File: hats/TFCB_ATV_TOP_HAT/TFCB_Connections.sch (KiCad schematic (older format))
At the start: 5 parts

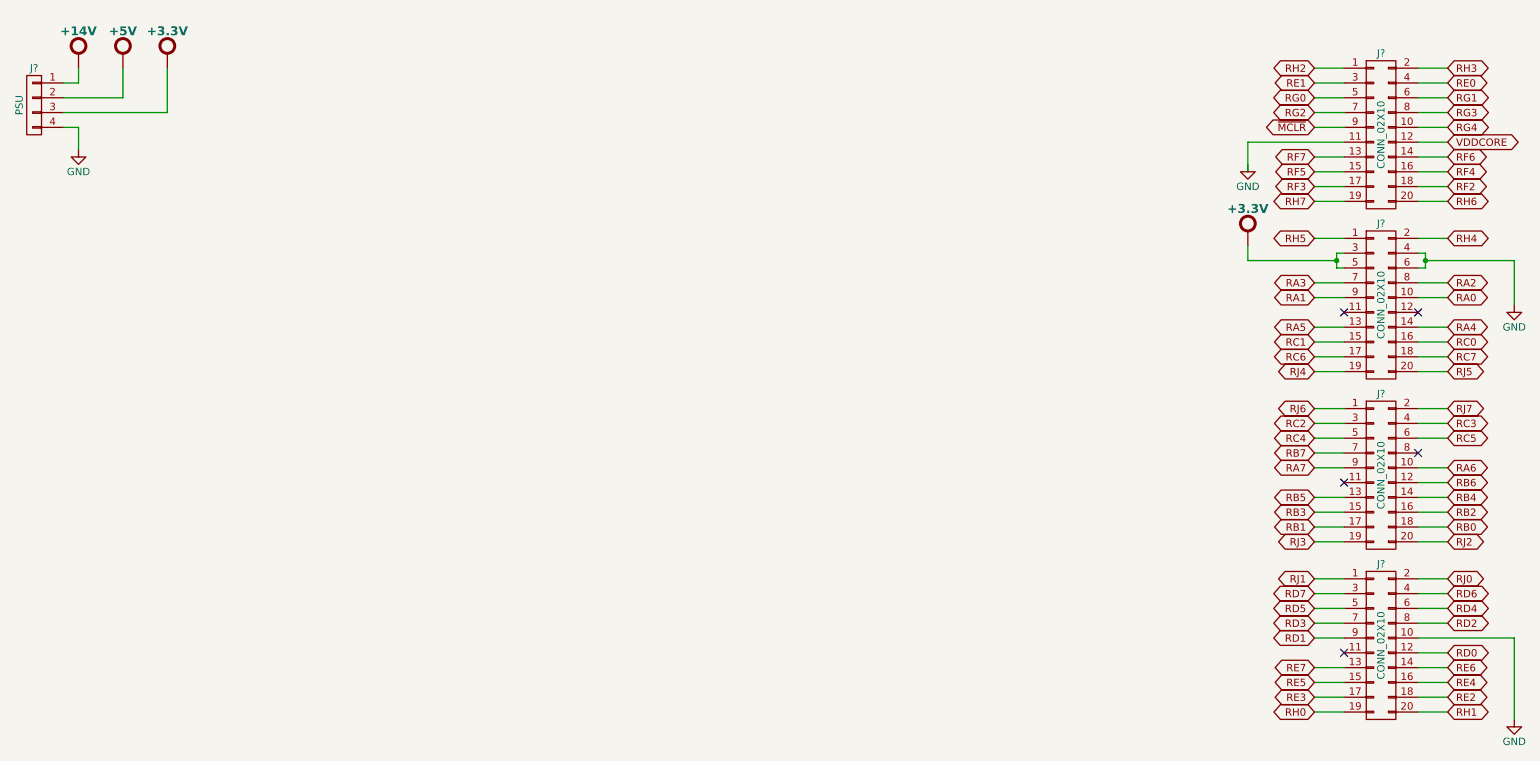
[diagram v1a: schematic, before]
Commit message: Added scanner trigger and current sense cct
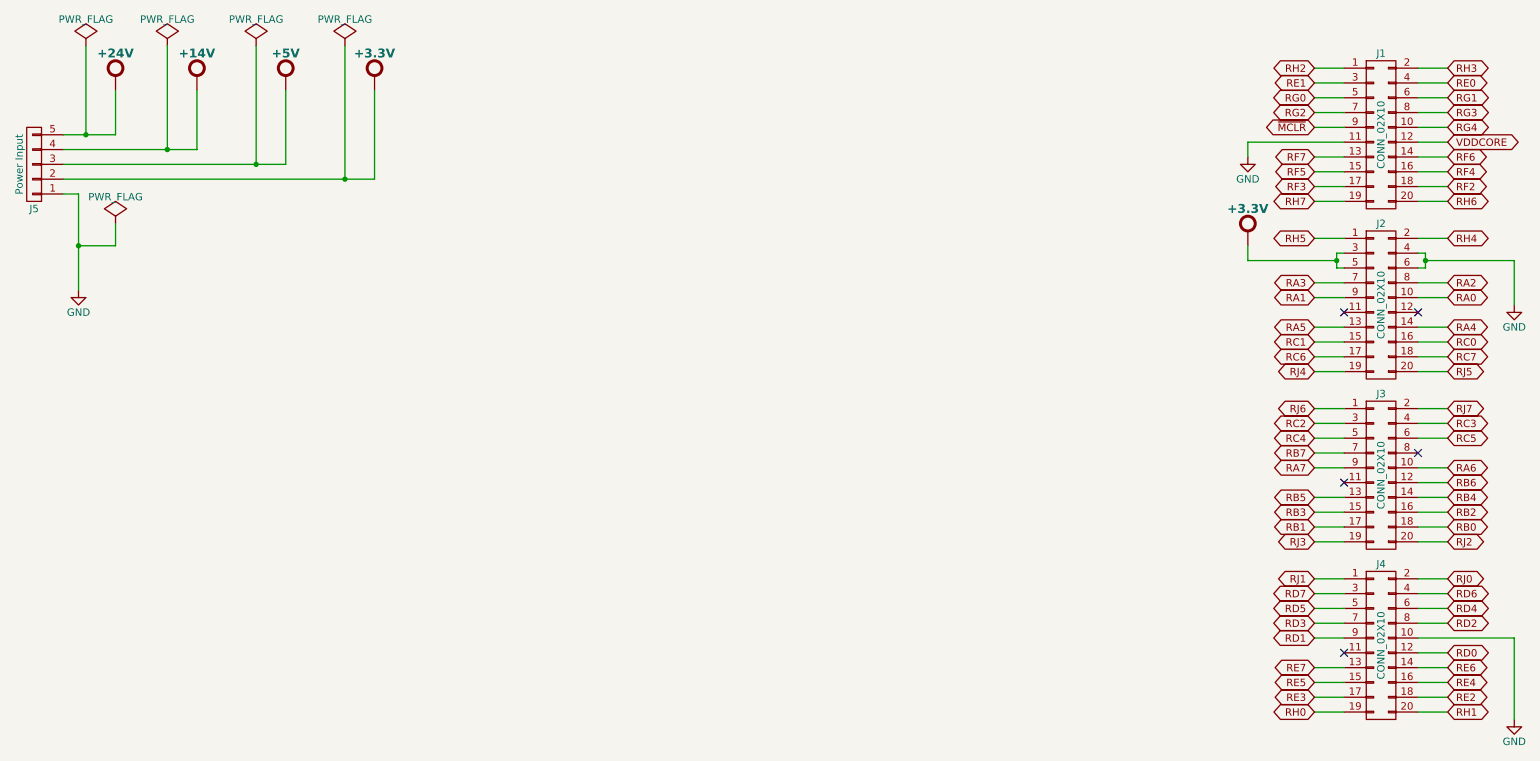
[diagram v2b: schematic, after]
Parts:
- removed J?: PSU, symbol CONN_01X04
- added J5: Power Input, bjh-kicad-connector-fp:Weidmuller-SL-5.08-Vertical-5Pole, symbol CONN_01X05
- J1, J2, J3, J4: renamed from J?; footprint (none) -> bjh-kicad-connector-fp:RCPT-2row-2.54mm-10way
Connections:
- net +14V: now also J5.4 (P4)
- net +3.3V: now also J5.2 (P2)
- net +5V: now also J5.3 (P3)
- net GND: now also J1.11 (P11), J5.1 (P1)
- new net +24V: J5.5 (P5)
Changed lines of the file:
@@
 LIBS:contrib
 LIBS:valves
+LIBS:buzzer
+LIBS:Relays
+LIBS:PowerSymbols-BJH
+LIBS:Oscillators-BJH
+LIBS:Microchip-BJH
+LIBS:LCD-BJH
+LIBS:Devices-BJH
+LIBS:Connectors-BJH
 LIBS:Basics-BJH
-LIBS:buzzer
-LIBS:Connectors-BJH
-LIBS:Devices-BJH
-LIBS:LCD-BJH
-LIBS:Microchip-BJH
-LIBS:Oscillators-BJH
-LIBS:PowerSymbols-BJH
-LIBS:Relays
+LIBS:Transistors-BJH
 LIBS:TFCB_ATV_HAT-cache
 EELAYER 25 0
@@
 $Descr A4 11693 8268
 encoding utf-8
-Sheet 2 7
+Sheet 2 6
 Title "TFCB CONNECTIONS"
 Date "Wed 24 Jun 2015"
@@
 $EndDescr
 $Comp
-L CONN_02X10 J?
+L CONN_02X10 J1
 U 1 1 558930FC
 P 9800 1350
-F 0 "J?" H 9800 1900 50  0000 C CNN
+F 0 "J1" H 9800 1900 50  0000 C CNN
 F 1 "CONN_02X10" V 9800 1350 50  0000 C CNN
-F 2 "" H 9800 150 60  0000 C CNN
+F 2 "bjh-kicad-connector-fp:RCPT-2row-2.54mm-10way" H 9800 150 60  0001 C CNN
 F 3 "" H 9800 150 60  0000 C CNN
 	1    9800 1350
@@
 $EndComp
 $Comp
-L CONN_02X10 J?
+L CONN_02X10 J2
 U 1 1 558931C8
 P 9800 2500
-F 0 "J?" H 9800 3050 50  0000 C CNN
+F 0 "J2" H 9800 3050 50  0000 C CNN
 F 1 "CONN_02X10" V 9800 2500 50  0000 C CNN
-F 2 "" H 9800 1300 60  0000 C CNN
+F 2 "bjh-kicad-connector-fp:RCPT-2row-2.54mm-10way" H 9800 1300 60  0001 C CNN
 F 3 "" H 9800 1300 60  0000 C CNN
 	1    9800 2500
@@
 $EndComp
 $Comp
-L CONN_02X10 J?
+L CONN_02X10 J3
 U 1 1 5589321A
 P 9800 3650
-F 0 "J?" H 9800 4200 50  0000 C CNN
+F 0 "J3" H 9800 4200 50  0000 C CNN
 F 1 "CONN_02X10" V 9800 3650 50  0000 C CNN
-F 2 "" H 9800 2450 60  0000 C CNN
+F 2 "bjh-kicad-connector-fp:RCPT-2row-2.54mm-10way" H 9800 2450 60  0001 C CNN
 F 3 "" H 9800 2450 60  0000 C CNN
 	1    9800 3650
@@
 $EndComp
 $Comp
-L CONN_02X10 J?
+L CONN_02X10 J4
 U 1 1 55893262
 P 9800 4800
-F 0 "J?" H 9800 5350 50  0000 C CNN
+F 0 "J4" H 9800 5350 50  0000 C CNN
 F 1 "CONN_02X10" V 9800 4800 50  0000 C CNN
-F 2 "" H 9800 3600 60  0000 C CNN
+F 2 "bjh-kicad-connector-fp:RCPT-2row-2.54mm-10way" H 9800 3600 60  0001 C CNN
 F 3 "" H 9800 3600 60  0000 C CNN
 	1    9800 4800
@@
 RH1
 $Comp
-L GND #PWR?
+L GND #PWR01
 U 1 1 55894D4F
 P 10700 5300
-F 0 "#PWR?" H 10700 5050 50  0001 C CNN
+F 0 "#PWR01" H 10700 5050 50  0001 C CNN
 F 1 "GND" H 10700 5150 50  0000 C CNN
 F 2 "" H 10700 5300 60  0000 C CNN
@@
 $EndComp
 $Comp
-L GND #PWR?
+L GND #PWR02
 U 1 1 55894EE0
 P 10700 2500
-F 0 "#PWR?" H 10700 2250 50  0001 C CNN
+F 0 "#PWR02" H 10700 2250 50  0001 C CNN
 F 1 "GND" H 10700 2350 50  0000 C CNN
 F 2 "" H 10700 2500 60  0000 C CNN
@@
 $EndComp
 $Comp
-L +3.3V_BJH #PWR?
+L +3.3V_BJH #PWR03
 U 1 1 558AB965
 P 8900 2050
-F 0 "#PWR?" H 8900 2240 20  0001 C CNN
+F 0 "#PWR03" H 8900 2240 20  0001 C CNN
 F 1 "+3.3V_BJH" H 8900 2240 51  0001 C CNN
 F 2 "" H 8900 2050 60  0001 C CNN
@@
 	1    0    0    -1
 $EndComp
+$Comp
+L GND #PWR04
+U 1 1 558ABA4F
+P 8900 1500
+F 0 "#PWR04" H 8900 1250 50  0001 C CNN
+F 1 "GND" H 8900 1350 50  0000 C CNN
+F 2 "" H 8900 1500 60  0000 C CNN
+F 3 "" H 8900 1500 60  0000 C CNN
+	1    8900 1500
+	1    0    0    -1
+$EndComp
+$Comp
+L +14V_BJH #PWR05
+U 1 1 558ABE2B
+P 1800 1000
+F 0 "#PWR05" H 1800 1190 20  0001 C CNN
+F 1 "+14V_BJH" H 1800 1190 51  0001 C CNN
+F 2 "" H 1800 1000 60  0001 C CNN
+F 3 "" H 1800 1000 60  0001 C CNN
+F 4 "+14V" H 1800 1200 60  0000 C CNB "NAME"
+	1    1800 1000
+	1    0    0    -1
+$EndComp
+$Comp
+L +5V_BJH #PWR06
+U 1 1 558ABE4F
+P 2400 1000
+F 0 "#PWR06" H 2400 1190 20  0001 C CNN
+F 1 "+5V_BJH" H 2400 1190 51  0001 C CNN
+F 2 "" H 2400 1000 60  0001 C CNN
+F 3 "" H 2400 1000 60  0001 C CNN
+F 4 "+5V" H 2400 1200 60  0000 C CNB "NAME"
+	1    2400 1000
+	1    0    0    -1
+$EndComp
+$Comp
+L +3.3V_BJH #PWR07
+U 1 1 558ABE73
+P 3000 1000
+F 0 "#PWR07" H 3000 1190 20  0001 C CNN
+F 1 "+3.3V_BJH" H 3000 1190 51  0001 C CNN
+F 2 "" H 3000 1000 60  0001 C CNN
+F 3 "" H 3000 1000 60  0001 C CNN
+F 4 "+3.3V" H 3000 1200 60  0000 C CNB "NAME"
+	1    3000 1000
+	1    0    0    -1
+$EndComp
+$Comp
+L GND #PWR08
+U 1 1 558ABF2A
+P 1000 2400
+F 0 "#PWR08" H 1000 2150 50  0001 C CNN
+F 1 "GND" H 1000 2250 50  0000 C CNN
+F 2 "" H 1000 2400 60  0000 C CNN
+F 3 "" H 1000 2400 60  0000 C CNN
+	1    1000 2400
+	1    0    0    -1
+$EndComp
 Wire Wire Line
 	9350 900  9550 900
@@
 	8900 2200 9500 2200
 Connection ~ 9500 2200
-$Comp
-L GND #PWR?
-U 1 1 558ABA4F
-P 8900 1550
-F 0 "#PWR?" H 8900 1300 50  0001 C CNN
-F 1 "GND" H 8900 1400 50  0000 C CNN
-F 2 "" H 8900 1550 60  0000 C CNN
-F 3 "" H 8900 1550 60  0000 C CNN
-	1    8900 1550
-	1    0    0    -1
-$EndComp
-Wire Wire Line
-	8900 1600 8900 1400
 Wire Wire Line
 	8900 1400 9550 1400
-$Comp
-L CONN_01X04 J?
-U 1 1 558ABD6E
-P 700 1150
-F 0 "J?" H 700 1400 50  0000 C CNN
-F 1 "PSU" V 800 1150 50  0000 C CNN
-F 2 "" H 700 1150 60  0000 C CNN
-F 3 "" H 700 1150 60  0000 C CNN
-	1    700  1150
-	-1   0    0    -1
-$EndComp
-$Comp
-L +14V_BJH #PWR?
-U 1 1 558ABE2B
-P 1000 850
-F 0 "#PWR?" H 1000 1040 20  0001 C CNN
-F 1 "+14V_BJH" H 1000 1040 51  0001 C CNN
-F 2 "" H 1000 850 60  0001 C CNN
-F 3 "" H 1000 850 60  0001 C CNN
-F 4 "+14V" H 1000 1050 60  0000 C CNB "NAME"
-	1    1000 850
-	1    0    0    -1
-$EndComp
-$Comp
-L +5V_BJH #PWR?
-U 1 1 558ABE4F
-P 1300 850
-F 0 "#PWR?" H 1300 1040 20  0001 C CNN
-F 1 "+5V_BJH" H 1300 1040 51  0001 C CNN
-F 2 "" H 1300 850 60  0001 C CNN
-F 3 "" H 1300 850 60  0001 C CNN
-F 4 "+5V" H 1300 1050 60  0000 C CNB "NAME"
-	1    1300 850
-	1    0    0    -1
-$EndComp
-$Comp
-L +3.3V_BJH #PWR?
-U 1 1 558ABE73
-P 1600 850
-F 0 "#PWR?" H 1600 1040 20  0001 C CNN
-F 1 "+3.3V_BJH" H 1600 1040 51  0001 C CNN
-F 2 "" H 1600 850 60  0001 C CNN
-F 3 "" H 1600 850 60  0001 C CNN
-F 4 "+3.3V" H 1600 1050 60  0000 C CNB "NAME"
-	1    1600 850
-	1    0    0    -1
-$EndComp
-$Comp
-L GND #PWR?
-U 1 1 558ABF2A
-P 1000 1450
-F 0 "#PWR?" H 1000 1200 50  0001 C CNN
-F 1 "GND" H 1000 1300 50  0000 C CNN
-F 2 "" H 1000 1450 60  0000 C CNN
-F 3 "" H 1000 1450 60  0000 C CNN
-	1    1000 1450
-	1    0    0    -1
-$EndComp
-Wire Wire Line
-	900  1300 1000 1300
-Wire Wire Line
-	1000 1300 1000 1450
-Wire Wire Line
-	1000 900  1000 1000
-Wire Wire Line
-	1000 1000 900  1000
-Wire Wire Line
-	1300 900  1300 1100
-Wire Wire Line
-	1300 1100 900  1100
-Wire Wire Line
-	1600 900  1600 1200
-Wire Wire Line
-	1600 1200 900  1200
+Wire Wire Line
+	900  1750 1000 1750
+Wire Wire Line
+	1000 1750 1000 2400
+Wire Wire Line
+	900  1450 1800 1450
+Wire Wire Line
+	900  1550 2400 1550
+Wire Wire Line
+	900  1650 3000 1650
+Wire Wire Line
+	1800 1450 1800 1050
+Wire Wire Line
+	2400 1550 2400 1050
+Wire Wire Line
+	3000 1650 3000 1050
+$Comp
+L PWR_FLAG #FLG09
+U 1 1 55B023D2
+P 1600 750
+F 0 "#FLG09" H 1600 845 50  0001 C CNN
+F 1 "PWR_FLAG" H 1600 930 50  0000 C CNN
+F 2 "" H 1600 750 60  0000 C CNN
+F 3 "" H 1600 750 60  0000 C CNN
+	1    1600 750
+	1    0    0    -1
+$EndComp
+Wire Wire Line
+	1600 750  1600 1450
+Connection ~ 1600 1450
+$Comp
+L PWR_FLAG #FLG010
+U 1 1 55B02455
+P 2200 750
+F 0 "#FLG010" H 2200 845 50  0001 C CNN
+F 1 "PWR_FLAG" H 2200 930 50  0000 C CNN
+F 2 "" H 2200 750 60  0000 C CNN
+F 3 "" H 2200 750 60  0000 C CNN
+	1    2200 750
+	1    0    0    -1
+$EndComp
+$Comp
+L PWR_FLAG #FLG011
+U 1 1 55B02473
+P 2800 750
+F 0 "#FLG011" H 2800 845 50  0001 C CNN
+F 1 "PWR_FLAG" H 2800 930 50  0000 C CNN
+F 2 "" H 2800 750 60  0000 C CNN
+F 3 "" H 2800 750 60  0000 C CNN
+	1    2800 750
+	1    0    0    -1
+$EndComp
+Wire Wire Line
+	2200 750  2200 1550
+Connection ~ 2200 1550
+Wire Wire Line
+	2800 750  2800 1650
+Connection ~ 2800 1650
+$Comp
+L PWR_FLAG #FLG012
+U 1 1 55B026DF
+P 1250 1950
+F 0 "#FLG012" H 1250 2045 50  0001 C CNN
+F 1 "PWR_FLAG" H 1250 2130 50  0000 C CNN
+F 2 "" H 1250 1950 60  0000 C CNN
+F 3 "" H 1250 1950 60  0000 C CNN
+	1    1250 1950
+	1    0    0    -1
+$EndComp
+Wire Wire Line
+	1250 1950 1250 2100
+Wire Wire Line
+	1250 2100 1000 2100
+Connection ~ 1000 2100
+Wire Wire Line
+	8900 1400 8900 1500
+$Comp
+L CONN_01X05 J5
+U 1 1 55B22208
+P 700 1550
+F 0 "J5" H 700 1850 50  0000 C CNN
+F 1 "Power Input" V 800 1550 50  0000 C CNN
+F 2 "bjh-kicad-connector-fp:Weidmuller-SL-5.08-Vertical-5Pole" H 700 1550 60  0001 C CNN
+F 3 "" H 700 1550 60  0000 C CNN
+	1    700  1550
+	-1   0    0    1
+$EndComp
+$Comp
+L +24V_BJH #PWR013
+U 1 1 55B222AA
+P 1250 1000
+F 0 "#PWR013" H 1250 1190 20  0001 C CNN
+F 1 "+24V_BJH" H 1250 1190 51  0001 C CNN
+F 2 "" H 1250 1000 60  0001 C CNN
+F 3 "" H 1250 1000 60  0001 C CNN
+F 4 "+24V" H 1250 1200 60  0000 C CNB "NAME"
+	1    1250 1000
+	1    0    0    -1
+$EndComp
+Wire Wire Line
+	1250 1050 1250 1350
+Wire Wire Line
+	1250 1350 900  1350
+$Comp
+L PWR_FLAG #FLG014
+U 1 1 55B225DA
+P 1050 750
+F 0 "#FLG014" H 1050 845 50  0001 C CNN
+F 1 "PWR_FLAG" H 1050 930 50  0000 C CNN
+F 2 "" H 1050 750 60  0000 C CNN
+F 3 "" H 1050 750 60  0000 C CNN
+	1    1050 750
+	1    0    0    -1
+$EndComp
+Wire Wire Line
+	1050 750  1050 1350
+Connection ~ 1050 1350
 $EndSCHEMATC

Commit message: More work on TFCB
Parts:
- removed J5: Power Input, bjh-kicad-connector-fp:Weidmuller-SL-5.08-Vertical-5Pole, symbol CONN_01X05
- added J5: POWER, bjh-kicad-connector-fp:Weidmuller-SL-5.08-Vertical-4Pole, symbol CONN_01X04
- added J6: 24V, bjh-kicad-connector-fp:Weidmuller-SL-5.08-Vertical-2Pole, symbol CONN_01X02
- J1, J2, J3, J4: footprint bjh-kicad-connector-fp:RCPT-2row-2.54mm-10way -> bjh-kicad-connector-fp:RCPT-2row-2.54mm-20way
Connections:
- net +14V: now also J5.1 (P1)
- net +24V: now also J6.1 (P1)
- net +3.3V: now also J2.4 (P4), J2.6 (P6), J5.3 (P3); no longer J2.3 (P3), J2.5 (P5)
- net +5V: now also J5.2 (P2)
- net GND: now also J1.12 (P12), J2.3 (P3), J2.5 (P5), J4.9 (P9), J5.4 (P4), J6.2 (P2); no longer J1.11 (P11), J2.4 (P4), J2.6 (P6), J4.10 (P10)
- net RA0: now also J2.9 (P9); no longer J2.10 (P10)
- net RA1: now also J2.10 (P10); no longer J2.9 (P9)
- net RA2: now also J2.7 (P7); no longer J2.8 (P8)
- net RA3: now also J2.8 (P8); no longer J2.7 (P7)
- net RA4: now also J2.13 (P13); no longer J2.14 (P14)
- net RA5: now also J2.14 (P14); no longer J2.13 (P13)
- net RA6: now also J3.9 (P9); no longer J3.10 (P10)
- net RA7: now also J3.10 (P10); no longer J3.9 (P9)
- net RB0: now also J3.17 (P17); no longer J3.18 (P18)
- net RB1: now also J3.18 (P18); no longer J3.17 (P17)
- net RB2: now also J3.15 (P15); no longer J3.16 (P16)
- net RB3: now also J3.16 (P16); no longer J3.15 (P15)
- net RB4: now also J3.13 (P13); no longer J3.14 (P14)
- net RB5: now also J3.14 (P14); no longer J3.13 (P13)
- net RB6: now also J3.11 (P11); no longer J3.12 (P12)
- net RB7: now also J3.8 (P8); no longer J3.7 (P7)
- net RC0: now also J2.15 (P15); no longer J2.16 (P16)
- net RC1: now also J2.16 (P16); no longer J2.15 (P15)
- net RC2: now also J3.4 (P4); no longer J3.3 (P3)
- net RC3: now also J3.3 (P3); no longer J3.4 (P4)
- net RC4: now also J3.6 (P6); no longer J3.5 (P5)
- net RC5: now also J3.5 (P5); no longer J3.6 (P6)
- net RC6: now also J2.18 (P18); no longer J2.17 (P17)
- net RC7: now also J2.17 (P17); no longer J2.18 (P18)
- net RD0: now also J4.11 (P11); no longer J4.12 (P12)
- net RD1: now also J4.10 (P10); no longer J4.9 (P9)
- net RD2: now also J4.7 (P7); no longer J4.8 (P8)
- net RD3: now also J4.8 (P8); no longer J4.7 (P7)
- net RD4: now also J4.5 (P5); no longer J4.6 (P6)
- net RD5: now also J4.6 (P6); no longer J4.5 (P5)
- net RD6: now also J4.3 (P3); no longer J4.4 (P4)
- net RD7: now also J4.4 (P4); no longer J4.3 (P3)
- net RE0: now also J1.3 (P3); no longer J1.4 (P4)
- net RE1: now also J1.4 (P4); no longer J1.3 (P3)
- net RE2: now also J4.17 (P17); no longer J4.18 (P18)
- net RE3: now also J4.18 (P18); no longer J4.17 (P17)
- net RE4: now also J4.15 (P15); no longer J4.16 (P16)
- net RE5: now also J4.16 (P16); no longer J4.15 (P15)
- net RE6: now also J4.13 (P13); no longer J4.14 (P14)
- net RE7: now also J4.14 (P14); no longer J4.13 (P13)
- net RF2: now also J1.17 (P17); no longer J1.18 (P18)
- net RF3: now also J1.18 (P18); no longer J1.17 (P17)
- net RF4: now also J1.15 (P15); no longer J1.16 (P16)
- net RF5: now also J1.16 (P16); no longer J1.15 (P15)
- net RF6: now also J1.13 (P13); no longer J1.14 (P14)
- net RF7: now also J1.14 (P14); no longer J1.13 (P13)
- net RG0: now also J1.6 (P6); no longer J1.5 (P5)
- net RG1: now also J1.5 (P5); no longer J1.6 (P6)
- net RG2: now also J1.8 (P8); no longer J1.7 (P7)
- net RG3: now also J1.7 (P7); no longer J1.8 (P8)
- net RG4: now also J1.9 (P9); no longer J1.10 (P10)
- net RH0: now also J4.20 (P20); no longer J4.19 (P19)
- net RH1: now also J4.19 (P19); no longer J4.20 (P20)
- net RH2: now also J1.2 (P2); no longer J1.1 (P1)
- net RH3: now also J1.1 (P1); no longer J1.2 (P2)
- net RH4: now also J2.1 (P1); no longer J2.2 (P2)
- net RH5: now also J2.2 (P2); no longer J2.1 (P1)
- net RH6: now also J1.19 (P19); no longer J1.20 (P20)
- net RH7: now also J1.20 (P20); no longer J1.19 (P19)
- net RJ0: now also J4.1 (P1); no longer J4.2 (P2)
- net RJ1: now also J4.2 (P2); no longer J4.1 (P1)
- net RJ2: now also J3.19 (P19); no longer J3.20 (P20)
- net RJ3: now also J3.20 (P20); no longer J3.19 (P19)
- net RJ4: now also J2.20 (P20); no longer J2.19 (P19)
- net RJ5: now also J2.19 (P19); no longer J2.20 (P20)
- net RJ6: now also J3.2 (P2); no longer J3.1 (P1)
- net RJ7: now also J3.1 (P1); no longer J3.2 (P2)
- net VDDCORE: now also J1.11 (P11); no longer J1.12 (P12)
- net ~MCLR: now also J1.10 (P10); no longer J1.9 (P9)
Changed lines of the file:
@@
 F 0 "J1" H 9800 1900 50  0000 C CNN
 F 1 "CONN_02X10" V 9800 1350 50  0000 C CNN
-F 2 "bjh-kicad-connector-fp:RCPT-2row-2.54mm-10way" H 9800 150 60  0001 C CNN
+F 2 "bjh-kicad-connector-fp:RCPT-2row-2.54mm-20way" H 9800 150 60  0001 C CNN
 F 3 "" H 9800 150 60  0000 C CNN
 	1    9800 1350
-	1    0    0    -1
+	-1   0    0    -1
 $EndComp
 $Comp
@@
 F 0 "J2" H 9800 3050 50  0000 C CNN
 F 1 "CONN_02X10" V 9800 2500 50  0000 C CNN
-F 2 "bjh-kicad-connector-fp:RCPT-2row-2.54mm-10way" H 9800 1300 60  0001 C CNN
+F 2 "bjh-kicad-connector-fp:RCPT-2row-2.54mm-20way" H 9800 1300 60  0001 C CNN
 F 3 "" H 9800 1300 60  0000 C CNN
 	1    9800 2500
-	1    0    0    -1
+	-1   0    0    -1
 $EndComp
 $Comp
@@
 F 0 "J3" H 9800 4200 50  0000 C CNN
 F 1 "CONN_02X10" V 9800 3650 50  0000 C CNN
-F 2 "bjh-kicad-connector-fp:RCPT-2row-2.54mm-10way" H 9800 2450 60  0001 C CNN
+F 2 "bjh-kicad-connector-fp:RCPT-2row-2.54mm-20way" H 9800 2450 60  0001 C CNN
 F 3 "" H 9800 2450 60  0000 C CNN
 	1    9800 3650
-	1    0    0    -1
+	-1   0    0    -1
 $EndComp
 $Comp
@@
 F 0 "J4" H 9800 5350 50  0000 C CNN
 F 1 "CONN_02X10" V 9800 4800 50  0000 C CNN
-F 2 "bjh-kicad-connector-fp:RCPT-2row-2.54mm-10way" H 9800 3600 60  0001 C CNN
+F 2 "bjh-kicad-connector-fp:RCPT-2row-2.54mm-20way" H 9800 3600 60  0001 C CNN
 F 3 "" H 9800 3600 60  0000 C CNN
 	1    9800 4800
-	1    0    0    -1
+	-1   0    0    -1
 $EndComp
 Text GLabel 9350 900  0    50   BiDi ~ 0
@@
 	8900 1400 8900 1500
 $Comp
-L CONN_01X05 J5
-U 1 1 55B22208
-P 700 1550
-F 0 "J5" H 700 1850 50  0000 C CNN
-F 1 "Power Input" V 800 1550 50  0000 C CNN
-F 2 "bjh-kicad-connector-fp:Weidmuller-SL-5.08-Vertical-5Pole" H 700 1550 60  0001 C CNN
-F 3 "" H 700 1550 60  0000 C CNN
-	1    700  1550
-	-1   0    0    1
-$EndComp
-$Comp
 L +24V_BJH #PWR013
 U 1 1 55B222AA
-P 1250 1000
-F 0 "#PWR013" H 1250 1190 20  0001 C CNN
-F 1 "+24V_BJH" H 1250 1190 51  0001 C CNN
-F 2 "" H 1250 1000 60  0001 C CNN
-F 3 "" H 1250 1000 60  0001 C CNN
-F 4 "+24V" H 1250 1200 60  0000 C CNB "NAME"
-	1    1250 1000
-	1    0    0    -1
-$EndComp
-Wire Wire Line
-	1250 1050 1250 1350
-Wire Wire Line
-	1250 1350 900  1350
+P 1250 3300
+F 0 "#PWR013" H 1250 3490 20  0001 C CNN
+F 1 "+24V_BJH" H 1250 3490 51  0001 C CNN
+F 2 "" H 1250 3300 60  0001 C CNN
+F 3 "" H 1250 3300 60  0001 C CNN
+F 4 "+24V" H 1250 3500 60  0000 C CNB "NAME"
+	1    1250 3300
+	1    0    0    -1
+$EndComp
+Wire Wire Line
+	1250 3350 1250 3650
+Wire Wire Line
+	1250 3650 900  3650
 $Comp
 L PWR_FLAG #FLG014
 U 1 1 55B225DA
-P 1050 750
-F 0 "#FLG014" H 1050 845 50  0001 C CNN
-F 1 "PWR_FLAG" H 1050 930 50  0000 C CNN
-F 2 "" H 1050 750 60  0000 C CNN
-F 3 "" H 1050 750 60  0000 C CNN
-	1    1050 750
-	1    0    0    -1
-$EndComp
-Wire Wire Line
-	1050 750  1050 1350
-Connection ~ 1050 1350
+P 1050 3050
+F 0 "#FLG014" H 1050 3145 50  0001 C CNN
+F 1 "PWR_FLAG" H 1050 3230 50  0000 C CNN
+F 2 "" H 1050 3050 60  0000 C CNN
+F 3 "" H 1050 3050 60  0000 C CNN
+	1    1050 3050
+	1    0    0    -1
+$EndComp
+Wire Wire Line
+	1050 3050 1050 3650
+Connection ~ 1050 3650
+$Comp
+L CONN_01X04 J5
+U 1 1 55B8A23C
+P 700 1600
+F 0 "J5" H 700 1850 50  0000 C CNN
+F 1 "POWER" V 800 1600 50  0000 C CNN
+F 2 "bjh-kicad-connector-fp:Weidmuller-SL-5.08-Vertical-4Pole" H 700 1600 60  0001 C CNN
+F 3 "" H 700 1600 60  0000 C CNN
+	1    700  1600
+	-1   0    0    -1
+$EndComp
+$Comp
+L CONN_01X02 J6
+U 1 1 55B8A298
+P 700 3700
+F 0 "J6" H 700 3850 50  0000 C CNN
+F 1 "24V" V 800 3700 50  0000 C CNN
+F 2 "bjh-kicad-connector-fp:Weidmuller-SL-5.08-Vertical-2Pole" H 700 3700 60  0001 C CNN
+F 3 "" H 700 3700 60  0000 C CNN
+	1    700  3700
+	-1   0    0    -1
+$EndComp
+$Comp
+L GND #PWR015
+U 1 1 55B8A3EA
+P 1050 3900
+F 0 "#PWR015" H 1050 3650 50  0001 C CNN
+F 1 "GND" H 1050 3750 50  0000 C CNN
+F 2 "" H 1050 3900 60  0000 C CNN
+F 3 "" H 1050 3900 60  0000 C CNN
+	1    1050 3900
+	1    0    0    -1
+$EndComp
+Wire Wire Line
+	1050 3900 1050 3750
+Wire Wire Line
+	1050 3750 900  3750
 $EndSCHEMATC
